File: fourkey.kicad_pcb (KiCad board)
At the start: 2 copper layers, 85.3 x 77.7 mm, 27 parts, among them K1 KEYSW, K2 KEYSW, K3 KEYSW, K4 KEYSW, SW1 RESET, U1 ProMicro

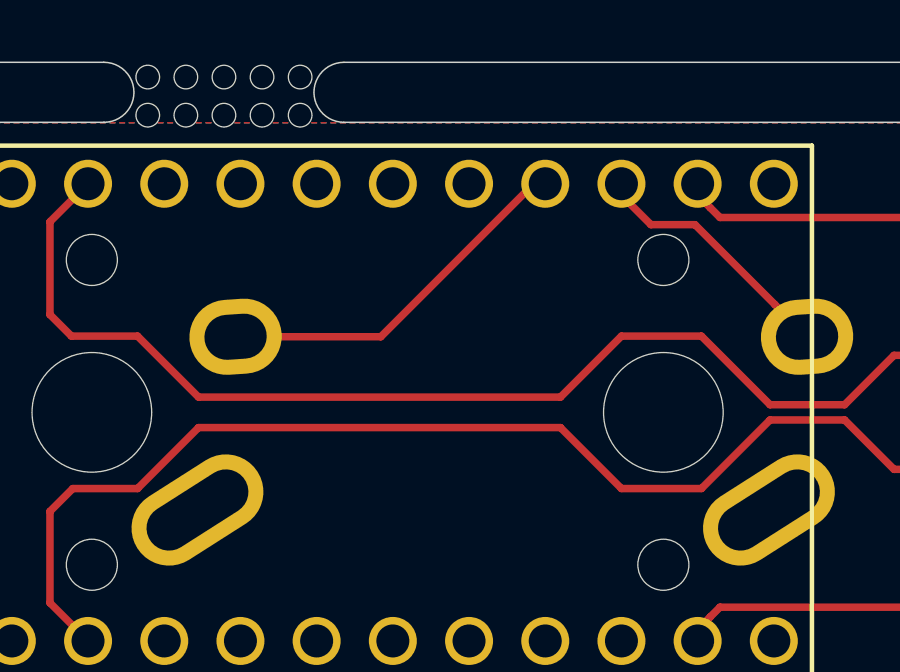
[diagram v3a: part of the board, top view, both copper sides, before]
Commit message: minor trace adjustments
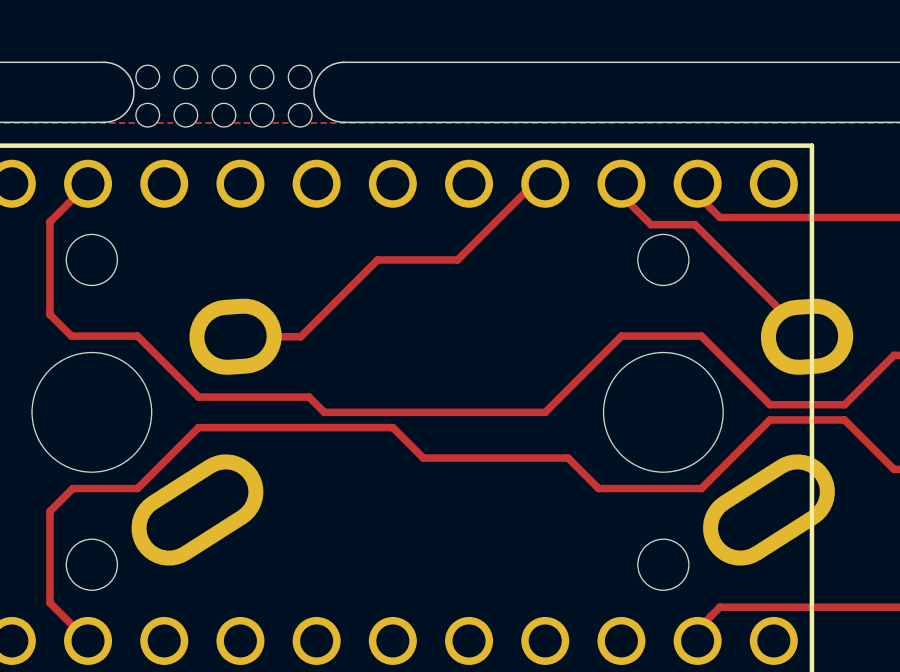
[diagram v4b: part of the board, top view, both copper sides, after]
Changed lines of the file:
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@@
     (thickness 1.6)
     (drawings 69)
-    (tracks 45)
+    (tracks 51)
     (zones 0)
     (modules 27)
@@
   (gr_line (start 67.564 69.834) (end 67.564 89.17) (layer Edge.Cuts) (width 0.05))
   (gr_line (start 144.78 69.834) (end 134.344 69.834) (layer Edge.Cuts) (width 0.05))
-  (segment (start 87.229 76.982) (end 92.329 71.882) (width 0.25) (layer F.Cu) (net 2))
-  (segment (start 82.387 76.982) (end 87.229 76.982) (width 0.25) (layer F.Cu) (net 2))
+  (segment (start 89.789 74.422) (end 92.329 71.882) (width 0.25) (layer F.Cu) (net 2))
+  (segment (start 84.562 76.982) (end 87.122 74.422) (width 0.25) (layer F.Cu) (net 2))
+  (segment (start 87.122 74.422) (end 89.789 74.422) (width 0.25) (layer F.Cu) (net 2))
+  (segment (start 82.387 76.982) (end 84.562 76.982) (width 0.25) (layer F.Cu) (net 2))
   (segment (start 97.701099 73.246099) (end 100.362469 75.907469) (width 0.25) (layer F.Cu) (net 3))
   (segment (start 96.233099 73.246099) (end 97.701099 73.246099) (width 0.25) (layer F.Cu) (net 3))
@@
   (segment (start 139.537 76.982) (end 123.297 76.982) (width 0.25) (layer F.Cu) (net 7))
   (segment (start 105.435 77.602) (end 111.735 77.602) (width 0.25) (layer F.Cu) (net 9))
-  (segment (start 104.335 77.602) (end 105.435 77.602) (width 0.25) (layer F.Cu) (net 9))
-  (segment (start 100.203 79.248) (end 102.689 79.248) (width 0.25) (layer F.Cu) (net 9))
+  (segment (start 102.689 79.248) (end 104.335 77.602) (width 0.25) (layer F.Cu) (net 9))
+  (segment (start 95.25 76.962) (end 97.917 76.962) (width 0.25) (layer F.Cu) (net 9))
+  (segment (start 76.2 76.244667) (end 76.917333 76.962) (width 0.25) (layer F.Cu) (net 9))
   (segment (start 76.917333 76.962) (end 79.121 76.962) (width 0.25) (layer F.Cu) (net 9))
   (segment (start 97.917 76.962) (end 100.203 79.248) (width 0.25) (layer F.Cu) (net 9))
-  (segment (start 95.25 76.962) (end 97.917 76.962) (width 0.25) (layer F.Cu) (net 9))
-  (segment (start 93.218 78.994) (end 95.25 76.962) (width 0.25) (layer F.Cu) (net 9))
+  (segment (start 85.344 79.502) (end 92.71 79.502) (width 0.25) (layer F.Cu) (net 9))
+  (segment (start 84.836 78.994) (end 85.344 79.502) (width 0.25) (layer F.Cu) (net 9))
+  (segment (start 104.335 77.602) (end 105.435 77.602) (width 0.25) (layer F.Cu) (net 9))
+  (segment (start 79.121 76.962) (end 81.153 78.994) (width 0.25) (layer F.Cu) (net 9))
+  (segment (start 92.71 79.502) (end 95.25 76.962) (width 0.25) (layer F.Cu) (net 9))
+  (segment (start 81.153 78.994) (end 84.836 78.994) (width 0.25) (layer F.Cu) (net 9))
+  (segment (start 100.203 79.248) (end 102.689 79.248) (width 0.25) (layer F.Cu) (net 9))
+  (segment (start 76.2 73.152) (end 76.2 76.244667) (width 0.25) (layer F.Cu) (net 9))
   (segment (start 77.47 71.882) (end 76.2 73.152) (width 0.25) (layer F.Cu) (net 9))
-  (segment (start 79.121 76.962) (end 81.153 78.994) (width 0.25) (layer F.Cu) (net 9))
-  (segment (start 81.153 78.994) (end 93.218 78.994) (width 0.25) (layer F.Cu) (net 9))
-  (segment (start 76.2 76.244667) (end 76.917333 76.962) (width 0.25) (layer F.Cu) (net 9))
-  (segment (start 102.689 79.248) (end 104.335 77.602) (width 0.25) (layer F.Cu) (net 9))
-  (segment (start 76.2 73.152) (end 76.2 76.244667) (width 0.25) (layer F.Cu) (net 9))
   (segment (start 106.535 81.402) (end 111.735 81.402) (width 0.25) (layer F.Cu) (net 10))
+  (segment (start 102.689 79.756) (end 104.335 81.402) (width 0.25) (layer F.Cu) (net 10))
+  (segment (start 100.203 79.756) (end 102.689 79.756) (width 0.25) (layer F.Cu) (net 10))
+  (segment (start 76.962 82.042) (end 79.121 82.042) (width 0.25) (layer F.Cu) (net 10))
+  (segment (start 97.917 82.042) (end 100.203 79.756) (width 0.25) (layer F.Cu) (net 10))
+  (segment (start 94.488 82.042) (end 97.917 82.042) (width 0.25) (layer F.Cu) (net 10))
+  (segment (start 93.472 81.026) (end 94.488 82.042) (width 0.25) (layer F.Cu) (net 10))
+  (segment (start 88.646 81.026) (end 93.472 81.026) (width 0.25) (layer F.Cu) (net 10))
+  (segment (start 81.153 80.01) (end 87.63 80.01) (width 0.25) (layer F.Cu) (net 10))
+  (segment (start 87.63 80.01) (end 88.646 81.026) (width 0.25) (layer F.Cu) (net 10))
+  (segment (start 79.121 82.042) (end 81.153 80.01) (width 0.25) (layer F.Cu) (net 10))
+  (segment (start 76.2 85.852) (end 76.2 82.804) (width 0.25) (layer F.Cu) (net 10))
+  (segment (start 76.2 82.804) (end 76.962 82.042) (width 0.25) (layer F.Cu) (net 10))
   (segment (start 104.335 81.402) (end 106.535 81.402) (width 0.25) (layer F.Cu) (net 10))
-  (segment (start 76.962 82.042) (end 79.121 82.042) (width 0.25) (layer F.Cu) (net 10))
-  (segment (start 76.2 82.804) (end 76.962 82.042) (width 0.25) (layer F.Cu) (net 10))
-  (segment (start 97.917 82.042) (end 100.203 79.756) (width 0.25) (layer F.Cu) (net 10))
-  (segment (start 95.25 82.042) (end 97.917 82.042) (width 0.25) (layer F.Cu) (net 10))
-  (segment (start 102.689 79.756) (end 104.335 81.402) (width 0.25) (layer F.Cu) (net 10))
-  (segment (start 81.153 80.01) (end 93.218 80.01) (width 0.25) (layer F.Cu) (net 10))
-  (segment (start 100.203 79.756) (end 102.689 79.756) (width 0.25) (layer F.Cu) (net 10))
-  (segment (start 93.218 80.01) (end 95.25 82.042) (width 0.25) (layer F.Cu) (net 10))
-  (segment (start 76.2 85.852) (end 76.2 82.804) (width 0.25) (layer F.Cu) (net 10))
-  (segment (start 79.121 82.042) (end 81.153 80.01) (width 0.25) (layer F.Cu) (net 10))
   (segment (start 77.47 87.122) (end 76.2 85.852) (width 0.25) (layer F.Cu) (net 10))
   (zone (net 0) (net_name "") (layer F.Cu) (hatch edge 0.508)

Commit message: adjust labels
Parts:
- removed HOLE_M2.6 (x2): VAL**, MountingHole:MountingHole_2.2mm_M2_DIN965
- added HOLE_M2.2: VAL**, MountingHole:MountingHole_2.2mm_M2_DIN965, F.Cu at (106.2, 94.2)
- added HOLE_M2.2: VAL**, MountingHole:MountingHole_2.2mm_M2_DIN965, F.Cu at (106.2, 43.7)
- HOLE_M2.2 (x3): renamed from HOLE_M2.6; moved to F.Cu
- renumbered HOLE_M2.6 to HOLE_M2.2
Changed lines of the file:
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@@
     (38 B.Mask user)
     (39 F.Mask user)
-    (40 Dwgs.User user hide)
+    (40 Dwgs.User user)
     (41 Cmts.User user)
     (42 Eco1.User user)
@@
     (tags "mounting hole 2.2mm no annular m2 din965")
     (attr virtual)
-    (fp_text reference HOLE_M2.6 (at 0 -4.5) (layer F.SilkS) hide
+    (fp_text reference HOLE_M2.2 (at 0 -4.5) (layer F.SilkS) hide
       (effects (font (size 1.524 1.524) (thickness 0.3048)))
     )
@@
     (tags "mounting hole 2.2mm no annular m2 din965")
     (attr virtual)
-    (fp_text reference HOLE_M2.6 (at 0 -4.5) (layer F.SilkS) hide
+    (fp_text reference HOLE_M2.2 (at 0 -4.5) (layer F.SilkS) hide
       (effects (font (size 1.524 1.524) (thickness 0.3048)))
     )
@@
     (tags "mounting hole 2.2mm no annular m2 din965")
     (attr virtual)
-    (fp_text reference HOLE_M2.6 (at 0 -4.5) (layer F.SilkS) hide
+    (fp_text reference HOLE_M2.2 (at 0 -4.5) (layer F.SilkS) hide
       (effects (font (size 1.524 1.524) (thickness 0.3048)))
     )
@@
     (tags "mounting hole 2.2mm no annular m2 din965")
     (attr virtual)
-    (fp_text reference HOLE_M2.6 (at 0 -4.5) (layer F.SilkS) hide
+    (fp_text reference HOLE_M2.2 (at 0 -4.5) (layer F.SilkS) hide
       (effects (font (size 1.524 1.524) (thickness 0.3048)))
     )
@@
     (tags "mounting hole 2.2mm no annular m2 din965")
     (attr virtual)
-    (fp_text reference HOLE_M2.6 (at 0 4.5) (layer B.SilkS) hide
+    (fp_text reference HOLE_M2.2 (at 0 4.5) (layer B.SilkS) hide
       (effects (font (size 1.524 1.524) (thickness 0.3048)) (justify mirror))
     )
@@
     (fp_circle (center 0 0) (end 2.15 0) (layer B.CrtYd) (width 0.05))
     (fp_circle (center 0 0) (end 1.9 0) (layer Cmts.User) (width 0.15))
-    (fp_text user %R (at 0.3 0) (layer B.Fab)
-      (effects (font (size 1 1) (thickness 0.15)) (justify mirror))
-    )
-    (pad 1 np_thru_hole circle (at 0 0) (size 2.2 2.2) (drill 2.2) (layers *.Cu *.Mask))
-  )
-  (module MountingHole:MountingHole_2.2mm_M2_DIN965 (layer B.Cu)
+    (fp_text user %R (at 0.3 0) (layer F.Fab)
+      (effects (font (size 1 1) (thickness 0.15)))
+    )
+    (pad 1 np_thru_hole circle (at 0 0) (size 2.2 2.2) (drill 2.2) (layers *.Cu *.Mask))
+  )
+  (module MountingHole:MountingHole_2.2mm_M2_DIN965 (layer F.Cu)
     (at 145.844 115.348)
     (descr "Mounting Hole 2.2mm, no annular, M2, DIN965")
     (tags "mounting hole 2.2mm no annular m2 din965")
     (attr virtual)
-    (fp_text reference HOLE_M2.6 (at 0 4.5) (layer B.SilkS) hide
-      (effects (font (size 1.524 1.524) (thickness 0.3048)) (justify mirror))
-    )
-    (fp_text value VAL** (at 0.05 7.25) (layer B.SilkS) hide
-      (effects (font (size 1.524 1.524) (thickness 0.3048)) (justify mirror))
-    )
-    (fp_circle (center 0 0) (end 2.15 0) (layer B.CrtYd) (width 0.05))
-    (fp_circle (center 0 0) (end 1.9 0) (layer Cmts.User) (width 0.15))
-    (fp_text user %R (at 0.3 0) (layer B.Fab)
-      (effects (font (size 1 1) (thickness 0.15)) (justify mirror))
-    )
-    (pad 1 np_thru_hole circle (at 0 0) (size 2.2 2.2) (drill 2.2) (layers *.Cu *.Mask))
-  )
-  (module MountingHole:MountingHole_2.2mm_M2_DIN965 (layer B.Cu)
+    (fp_text reference HOLE_M2.2 (at 0 -4.5) (layer F.SilkS) hide
+      (effects (font (size 1.524 1.524) (thickness 0.3048)))
+    )
+    (fp_text value VAL** (at 0.05 -7.25) (layer F.SilkS) hide
+      (effects (font (size 1.524 1.524) (thickness 0.3048)))
+    )
+    (fp_text user %R (at 0.3 0) (layer F.Fab)
+      (effects (font (size 1 1) (thickness 0.15)))
+    )
+    (fp_circle (center 0 0) (end 1.9 0) (layer Cmts.User) (width 0.15))
+    (fp_circle (center 0 0) (end 2.15 0) (layer F.CrtYd) (width 0.05))
+    (pad 1 np_thru_hole circle (at 0 0) (size 2.2 2.2) (drill 2.2) (layers *.Cu *.Mask))
+  )
+  (module MountingHole:MountingHole_2.2mm_M2_DIN965 (layer F.Cu)
     (at 66.5 94.17)
     (descr "Mounting Hole 2.2mm, no annular, M2, DIN965")
     (tags "mounting hole 2.2mm no annular m2 din965")
     (attr virtual)
-    (fp_text reference HOLE_M2.6 (at 0 4.5) (layer B.SilkS) hide
-      (effects (font (size 1.524 1.524) (thickness 0.3048)) (justify mirror))
-    )
-    (fp_text value VAL** (at 0.05 7.25) (layer B.SilkS) hide
-      (effects (font (size 1.524 1.524) (thickness 0.3048)) (justify mirror))
-    )
-    (fp_circle (center 0 0) (end 2.15 0) (layer B.CrtYd) (width 0.05))
-    (fp_circle (center 0 0) (end 1.9 0) (layer Cmts.User) (width 0.15))
-    (fp_text user %R (at 0.3 0) (layer B.Fab)
-      (effects (font (size 1 1) (thickness 0.15)) (justify mirror))
-    )
-    (pad 1 np_thru_hole circle (at 0 0) (size 2.2 2.2) (drill 2.2) (layers *.Cu *.Mask))
-  )
-  (module MountingHole:MountingHole_2.2mm_M2_DIN965 (layer B.Cu)
+    (fp_text reference HOLE_M2.2 (at 0 -4.5) (layer F.SilkS) hide
+      (effects (font (size 1.524 1.524) (thickness 0.3048)))
+    )
+    (fp_text value VAL** (at 0.05 -7.25) (layer F.SilkS) hide
+      (effects (font (size 1.524 1.524) (thickness 0.3048)))
+    )
+    (fp_circle (center 0 0) (end 2.15 0) (layer F.CrtYd) (width 0.05))
+    (fp_circle (center 0 0) (end 1.9 0) (layer Cmts.User) (width 0.15))
+    (fp_text user %R (at 0.3 0) (layer F.Fab)
+      (effects (font (size 1 1) (thickness 0.15)))
+    )
+    (pad 1 np_thru_hole circle (at 0 0) (size 2.2 2.2) (drill 2.2) (layers *.Cu *.Mask))
+  )
+  (module MountingHole:MountingHole_2.2mm_M2_DIN965 (layer F.Cu)
     (at 145.844 94.17)
     (descr "Mounting Hole 2.2mm, no annular, M2, DIN965")
     (tags "mounting hole 2.2mm no annular m2 din965")
     (attr virtual)
-    (fp_text reference HOLE_M2.6 (at 0 4.5) (layer B.SilkS) hide
-      (effects (font (size 1.524 1.524) (thickness 0.3048)) (justify mirror))
-    )
-    (fp_text value VAL** (at 0.05 7.25) (layer B.SilkS) hide
-      (effects (font (size 1.524 1.524) (thickness 0.3048)) (justify mirror))
-    )
-    (fp_circle (center 0 0) (end 2.15 0) (layer B.CrtYd) (width 0.05))
-    (fp_circle (center 0 0) (end 1.9 0) (layer Cmts.User) (width 0.15))
-    (fp_text user %R (at 0.3 0) (layer B.Fab)
-      (effects (font (size 1 1) (thickness 0.15)) (justify mirror))
-    )
+    (fp_text reference HOLE_M2.2 (at 0 -4.5) (layer F.SilkS) hide
+      (effects (font (size 1.524 1.524) (thickness 0.3048)))
+    )
+    (fp_text value VAL** (at 0.05 -7.25) (layer F.SilkS) hide
+      (effects (font (size 1.524 1.524) (thickness 0.3048)))
+    )
+    (fp_text user %R (at 0.3 0) (layer F.Fab)
+      (effects (font (size 1 1) (thickness 0.15)))
+    )
+    (fp_circle (center 0 0) (end 1.9 0) (layer Cmts.User) (width 0.15))
+    (fp_circle (center 0 0) (end 2.15 0) (layer F.CrtYd) (width 0.05))
     (pad 1 np_thru_hole circle (at 0 0) (size 2.2 2.2) (drill 2.2) (layers *.Cu *.Mask))
   )
@@
     (tags "mounting hole 2.2mm no annular m2 din965")
     (attr virtual)
-    (fp_text reference HOLE_M2.6 (at 0 -4.5) (layer F.SilkS) hide
+    (fp_text reference HOLE_M2.2 (at 0 -4.5) (layer F.SilkS) hide
       (effects (font (size 1.524 1.524) (thickness 0.3048)))
     )
@@
     (tags "mounting hole 2.2mm no annular m2 din965")
     (attr virtual)
-    (fp_text reference HOLE_M2.6 (at 0 -4.5) (layer F.SilkS) hide
+    (fp_text reference HOLE_M2.2 (at 0 -4.5) (layer F.SilkS) hide
       (effects (font (size 1.524 1.524) (thickness 0.3048)))
     )
@@
     (tags "mounting hole 2.2mm no annular m2 din965")
     (attr virtual)
-    (fp_text reference HOLE_M2.6 (at 0 -4.5) (layer F.SilkS) hide
+    (fp_text reference HOLE_M2.2 (at 0 -4.5) (layer F.SilkS) hide
       (effects (font (size 1.524 1.524) (thickness 0.3048)))
     )
@@
     (tags "mounting hole 2.2mm no annular m2 din965")
     (attr virtual)
-    (fp_text reference HOLE_M2.6 (at 0 -4.5) (layer F.SilkS) hide
-      (effects (font (size 1.524 1.524) (thickness 0.3048)))
-    )
+    (fp_text reference HOLE_M2.2 (at 0 -4.5) (layer F.SilkS) hide
+      (effects (font (size 1.524 1.524) (thickness 0.3048)))
+    )

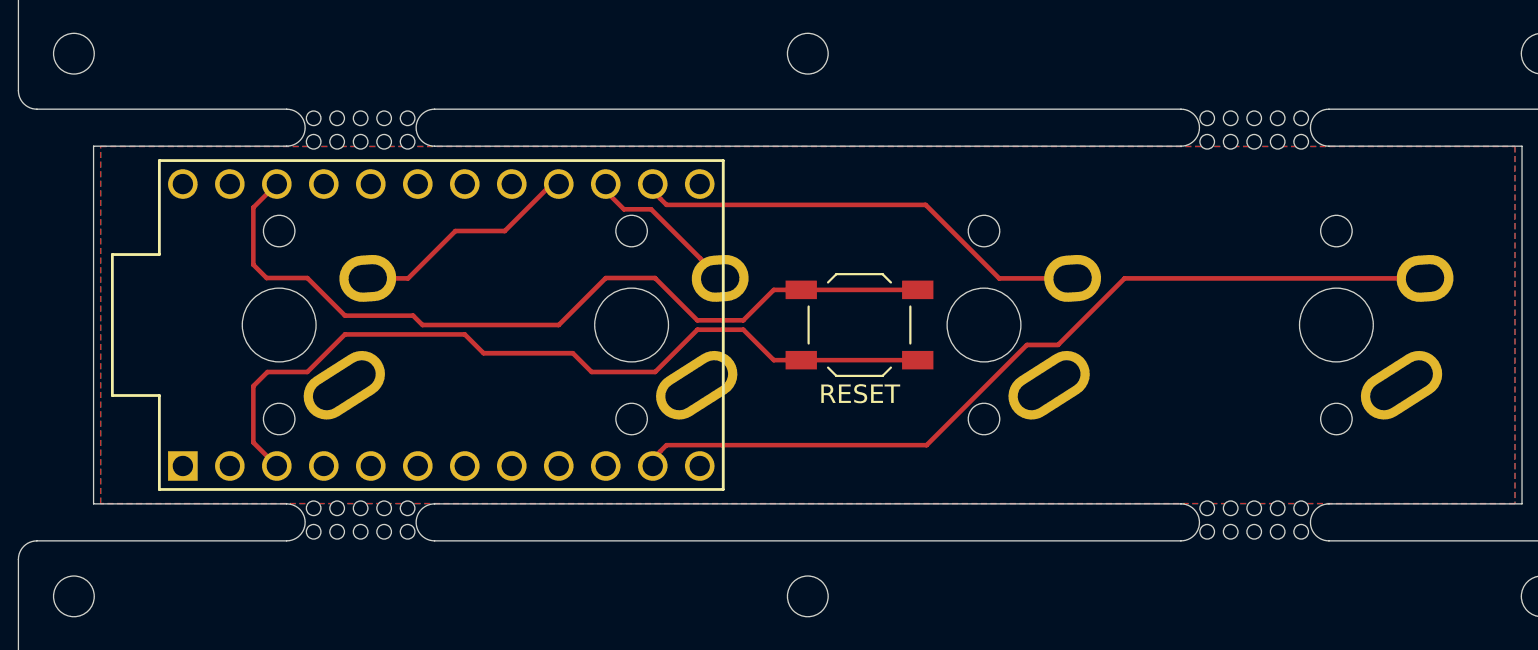
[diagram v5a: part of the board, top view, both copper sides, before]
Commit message: flip pro micro. remove one set of mousebites
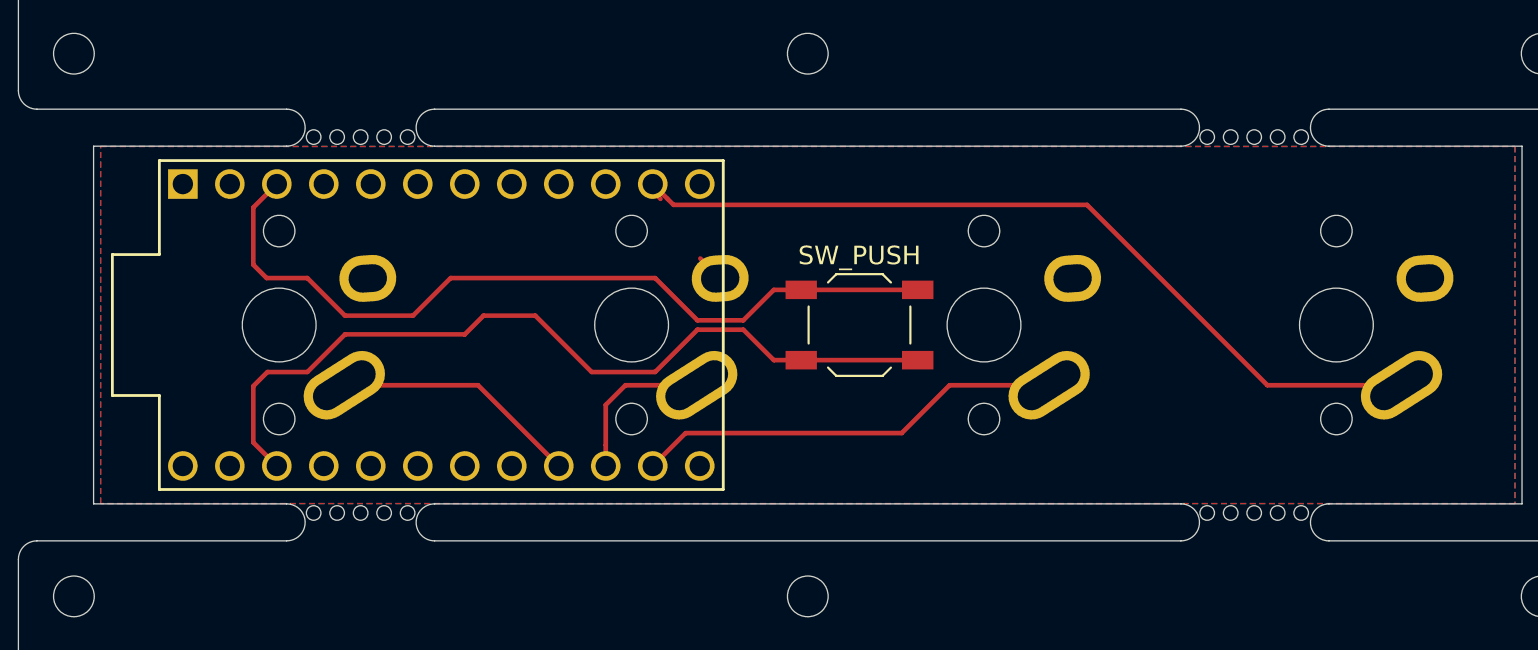
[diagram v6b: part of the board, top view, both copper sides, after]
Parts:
- removed the REF** at (82.0, 90.9)
- removed the REF** at (130.3, 90.9)
- removed the REF** at (130.3, 68.1)
- removed the REF** at (82.0, 68.1)
- removed the REF** at (130.3, 69.8)
- removed the REF** at (130.3, 89.2)
- removed the REF** at (82.0, 89.2)
- added REF**: breakaway-mousebites, Keebio-Parts:breakaway-mousebites, F.Cu at (130.3, 69.6)
- added REF**: breakaway-mousebites, Keebio-Parts:breakaway-mousebites, F.Cu at (130.3, 89.4)
- added REF**: breakaway-mousebites, Keebio-Parts:breakaway-mousebites, F.Cu at (82.0, 89.4)
- SW1: value RESET -> SW_PUSH
- U1: moved to B.Cu
- moved REF** 0.25 mm to (82.0, 69.6)
- turned SW1 to 180 degrees
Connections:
- K1 pad 1: Net-(K1-Pad1) -> /SW1
- K1 pad 2: /SW1 -> +5V
- K2 pad 1: Net-(K2-Pad1) -> /SW2
- K2 pad 2: /SW2 -> +5V
- K3 pad 1: Net-(K3-Pad1) -> /SW3
- K3 pad 2: /SW3 -> +5V
- K4 pad 1: Net-(K4-Pad1) -> /SW4
- K4 pad 2: /SW4 -> +5V
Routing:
- net /SW3: track 25.2 -> 23.2 mm
- net +5V: track 44.0 -> 45.6 mm
- net /SW1: track 12.1 -> 13.4 mm
